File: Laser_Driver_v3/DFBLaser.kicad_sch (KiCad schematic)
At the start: 38 parts, among them Q17 IRLML6344TRPBF, Q18 IRLML6344TRPBF, U23 OPA192IDR, U24 OPA192IDR

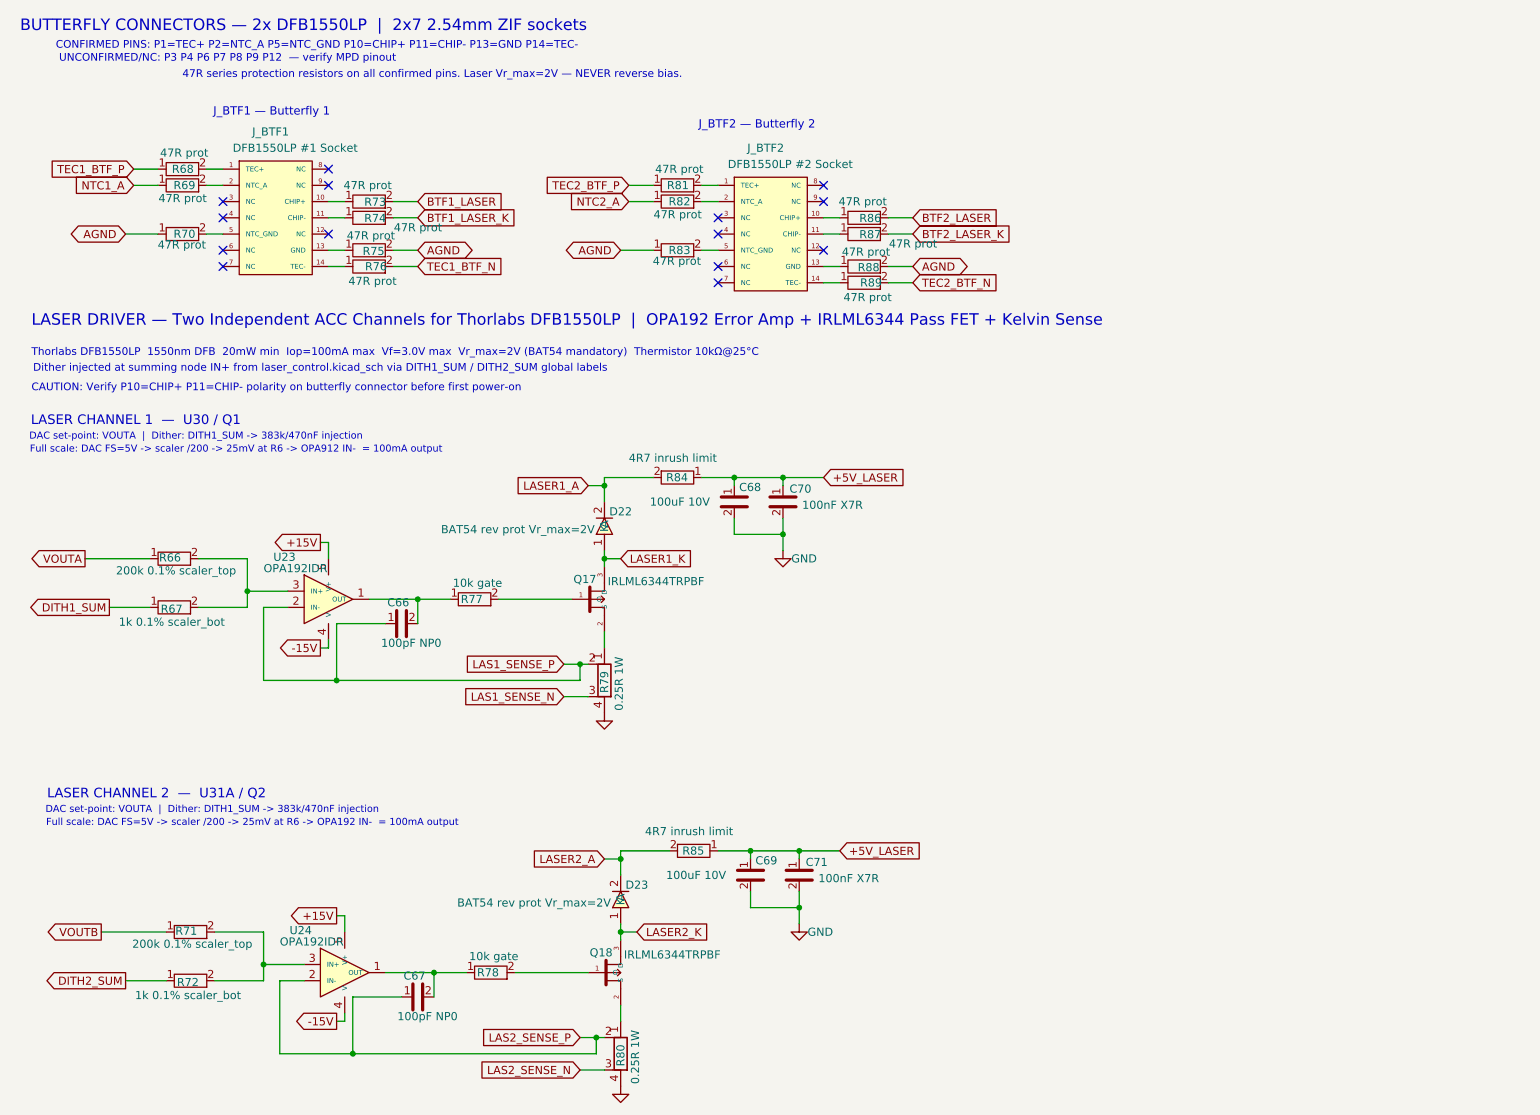
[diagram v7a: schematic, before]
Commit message: Many changes.  Working through ERC.
Main changes are for the grounds.  I found the NETTIE function to tie the GND, DGND and AGND together at a specific point on the boud with a footprint even.
Changed transformers one more time to be consistent for both.
Updated footprints to be consistent and avoid power input/output errors with the ERC.
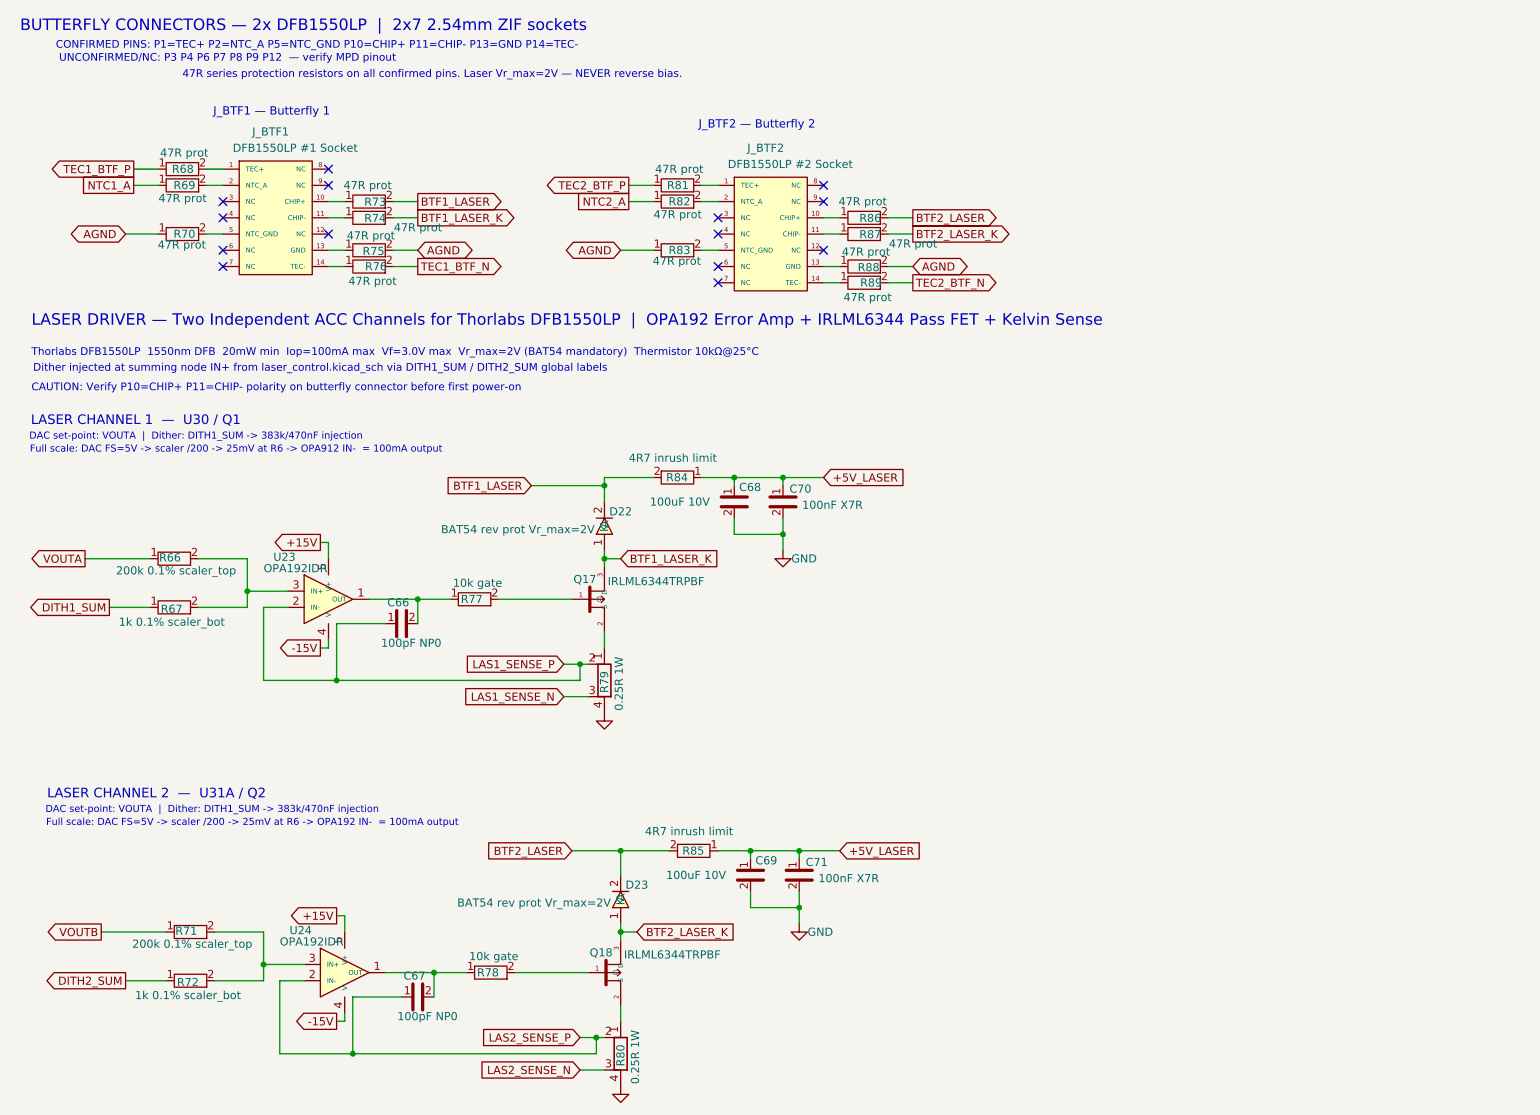
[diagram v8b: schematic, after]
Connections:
- net LASER1_A is gone; now on net BTF1_LASER: D22.2 (K), R84.2
- net LASER1_K is gone; now on net BTF1_LASER_K: D22.1 (A), Q17.3 (D)
- net LASER2_A is gone; now on net BTF2_LASER: D23.2 (K), R85.2
- net LASER2_K is gone; now on net BTF2_LASER_K: D23.1 (A), Q18.3 (D)
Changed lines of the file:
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@@
-	)
-	(junction
-		(at 109.22 146.05)
-		(diameter 0)
-		(color 0 0 0 0)
 	)
 	(junction
@@
 	)
 	(junction
+		(at 109.22 144.78)
+		(diameter 0)
+		(color 0 0 0 0)
+	)
+	(junction
 		(at 53.34 162.56)
 		(diameter 0)
@@
 	(wire
 		(pts
+			(xy 95.25 87.63) (xy 106.68 87.63)
+		)
+		(stroke
+			(width 0)
+			(type default)
+		)
+	)
+	(wire
+		(pts
+			(xy 101.6 144.78) (xy 109.22 144.78)
+		)
+		(stroke
+			(width 0)
+			(type default)
+		)
+	)
+	(wire
+		(pts
 			(xy 44.45 38.1) (xy 46.99 38.1)
 		)
@@
 	(wire
 		(pts
-			(xy 109.22 146.05) (xy 109.22 148.59)
-		)
-		(stroke
-			(width 0)
-			(type default)
-		)
-	)
-	(wire
-		(pts
 			(xy 72.39 109.22) (xy 64.77 109.22)
 		)
@@
 	(wire
 		(pts
-			(xy 106.68 146.05) (xy 109.22 146.05)
-		)
-		(stroke
-			(width 0)
-			(type default)
-		)
-	)
-	(wire
-		(pts
 			(xy 92.71 163.83) (xy 104.14 163.83)
 		)
@@
 	(wire
 		(pts
-			(xy 104.14 87.63) (xy 106.68 87.63)
-		)
-		(stroke
-			(width 0)
-			(type default)
-		)
-	)
-	(wire
-		(pts
 			(xy 55.88 176.53) (xy 67.31 176.53)
 		)
@@
 	(wire
 		(pts
-			(xy 109.22 144.78) (xy 109.22 146.05)
+			(xy 109.22 144.78) (xy 109.22 148.59)
 		)
 		(stroke
@@
 		)
 	)
-	(global_label "LASER1_K"
+	(global_label "BTF1_LASER_K"
 		(shape input)
 		(at 109.22 99.06 0)
@@
 		)
 		(property "Intersheetrefs" "${INTERSHEET_REFS}"
-			(at 121.3975 99.06 0)
+			(at 125.6913 99.06 0)
 			(hide yes)
 			(show_name no)
@@
 	)
 	(global_label "NTC1_A"
-		(shape input)
+		(shape passive)
 		(at 33.02 40.64 180)
 		(fields_autoplaced yes)
@@
 		)
 		(property "Intersheetrefs" "${INTERSHEET_REFS}"
-			(at 33.02 40.64 0)
+			(at 24.3123 40.64 0)
 			(hide yes)
 			(show_name no)
@@
 	)
 	(global_label "TEC2_BTF_N"
-		(shape input)
+		(shape output)
 		(at 154.94 55.88 0)
 		(fields_autoplaced yes)
@@
 		)
 		(property "Intersheetrefs" "${INTERSHEET_REFS}"
-			(at 154.94 55.88 0)
+			(at 169.1132 55.88 0)
 			(hide yes)
 			(show_name no)
@@
 	)
 	(global_label "TEC1_BTF_N"
-		(shape input)
+		(shape output)
 		(at 77.47 53.34 0)
 		(fields_autoplaced yes)
@@
 		)
 		(property "Intersheetrefs" "${INTERSHEET_REFS}"
-			(at 77.47 53.34 0)
+			(at 91.6432 53.34 0)
 			(hide yes)
 			(show_name no)
@@
 		)
 	)
-	(global_label "LASER2_K"
+	(global_label "BTF2_LASER_K"
 		(shape input)
 		(at 111.76 157.48 0)
@@
 		)
 		(property "Intersheetrefs" "${INTERSHEET_REFS}"
-			(at 123.9375 157.48 0)
+			(at 128.2313 157.48 0)
 			(hide yes)
 			(show_name no)
@@
 	)
 	(global_label "NTC2_A"
-		(shape input)
+		(shape passive)
 		(at 110.49 43.18 180)
 		(fields_autoplaced yes)
@@
 		)
 		(property "Intersheetrefs" "${INTERSHEET_REFS}"
-			(at 110.49 43.18 0)
+			(at 101.7823 43.18 0)
 			(hide yes)
 			(show_name no)
@@
 		)
 	)
+	(global_label "BTF2_LASER"
+		(shape input)
+		(at 101.6 144.78 180)
+		(fields_autoplaced yes)
+		(effects
+			(font
+				(size 1.27 1.27)
+			)
+			(justify right)
+		)
+		(property "Intersheetrefs" "${INTERSHEET_REFS}"
+			(at 87.3663 144.78 0)
+			(hide yes)
+			(show_name no)
+			(do_not_autoplace no)
+			(effects
+				(font
+					(size 1.27 1.27)
+				)
+				(justify right)
+			)
+		)
+	)
 	(global_label "AGND"
 		(shape bidirectional)
@@
 	)
 	(global_label "BTF1_LASER_K"
-		(shape input)
+		(shape output)
 		(at 77.47 45.72 0)
 		(fields_autoplaced yes)
@@
 		)
 		(property "Intersheetrefs" "${INTERSHEET_REFS}"
-			(at 77.47 45.72 0)
+			(at 93.9413 45.72 0)
 			(hide yes)
 			(show_name no)
@@
 				)
 				(justify left)
-			)
-		)
-	)
-	(global_label "LASER1_A"
-		(shape input)
-		(at 104.14 87.63 180)
-		(fields_autoplaced yes)
-		(effects
-			(font
-				(size 1.27 1.27)
-			)
-			(justify right)
-		)
-		(property "Intersheetrefs" "${INTERSHEET_REFS}"
-			(at 92.1439 87.63 0)
-			(hide yes)
-			(show_name no)
-			(do_not_autoplace no)
-			(effects
-				(font
-					(size 1.27 1.27)
-				)
-				(justify right)
 			)
 		)
@@
 	)
 	(global_label "BTF2_LASER"
-		(shape input)
+		(shape output)
 		(at 154.94 45.72 0)
 		(fields_autoplaced yes)
@@
 		)
 		(property "Intersheetrefs" "${INTERSHEET_REFS}"
-			(at 154.94 45.72 0)
+			(at 169.1737 45.72 0)
 			(hide yes)
 			(show_name no)
@@
 		)
 	)
+	(global_label "BTF1_LASER"
+		(shape input)
+		(at 95.25 87.63 180)
+		(fields_autoplaced yes)
+		(effects
+			(font
+				(size 1.27 1.27)
+			)
+			(justify right)
+		)
+		(property "Intersheetrefs" "${INTERSHEET_REFS}"
+			(at 81.0163 87.63 0)
+			(hide yes)
+			(show_name no)
+			(do_not_autoplace no)
+			(effects
+				(font
+					(size 1.27 1.27)
+				)
+				(justify right)
+			)
+		)
+	)
 	(global_label "AGND"
 		(shape bidirectional)
@@
 	)
 	(global_label "BTF1_LASER"
-		(shape input)
+		(shape output)
 		(at 77.47 43.18 0)
 		(fields_autoplaced yes)
@@
 		)
 		(property "Intersheetrefs" "${INTERSHEET_REFS}"
-			(at 77.47 43.18 0)
+			(at 91.7037 43.18 0)
 			(hide yes)
 			(show_name no)
@@
 	)
 	(global_label "BTF2_LASER_K"
-		(shape input)
+		(shape output)
 		(at 154.94 48.26 0)
 		(fields_autoplaced yes)
@@
 		)
 		(property "Intersheetrefs" "${INTERSHEET_REFS}"
-			(at 154.94 48.26 0)
+			(at 171.4113 48.26 0)
 			(hide yes)
 			(show_name no)
@@
 	)
 	(global_label "TEC2_BTF_P"
-		(shape input)
+		(shape output)
 		(at 110.49 40.64 180)
 		(fields_autoplaced yes)
@@
 		)
 		(property "Intersheetrefs" "${INTERSHEET_REFS}"
-			(at 110.49 40.64 0)
+			(at 96.3773 40.64 0)
 			(hide yes)
 			(show_name no)
@@
 		)
 	)
-	(global_label "LASER2_A"
-		(shape input)
-		(at 106.68 146.05 180)
+	(global_label "TEC1_BTF_P"
+		(shape output)
+		(at 33.02 38.1 180)
 		(fields_autoplaced yes)
 		(effects
@@
 		)
 		(property "Intersheetrefs" "${INTERSHEET_REFS}"
-			(at 94.6839 146.05 0)
-			(hide yes)
-			(show_name no)
-			(do_not_autoplace no)
-			(effects
-				(font
-					(size 1.27 1.27)
-				)
-				(justify right)
-			)
-		)
-	)
-	(global_label "TEC1_BTF_P"
-		(shape input)
-		(at 33.02 38.1 180)
-		(fields_autoplaced yes)
-		(effects
-			(font
-				(size 1.27 1.27)
-			)
-			(justify right)
-		)
-		(property "Intersheetrefs" "${INTERSHEET_REFS}"
-			(at 33.02 38.1 0)
-			(hide yes)
-			(show_name no)
+			(at 18.9073 38.1 0)
+			(hide yes)
+			(show_name no)
